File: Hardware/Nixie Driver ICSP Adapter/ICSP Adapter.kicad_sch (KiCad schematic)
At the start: 5 parts

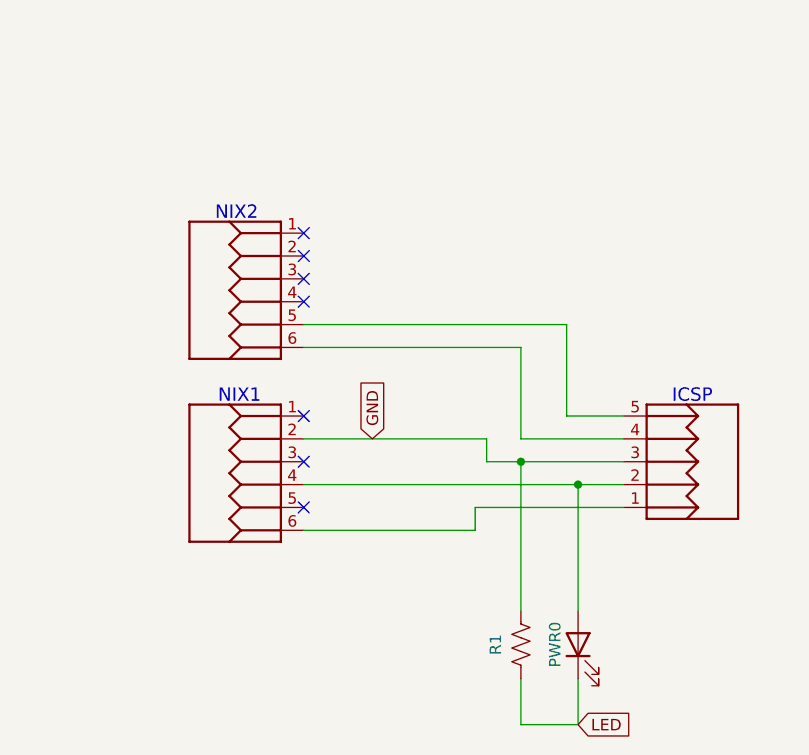
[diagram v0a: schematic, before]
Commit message: Converted to native KiCad footprints and symbols
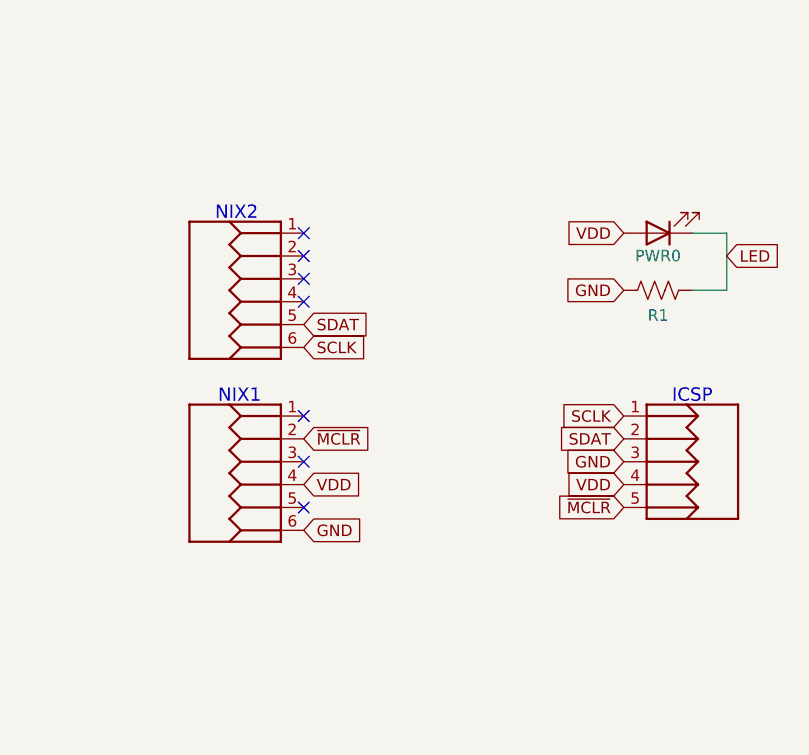
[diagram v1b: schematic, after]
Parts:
- ICSP0: footprint ICSP Adapter:HDR-1X5H -> Connector_PinHeader_2.54mm:PinHeader_1x05_P2.54mm_Horizontal
- NIX1, NIX2: footprint ICSP Adapter:HDRF-2X3 -> Connector_PinHeader_2.54mm:PinHeader_2x03_P2.54mm_Vertical
- PWR0: footprint ICSP Adapter:LED-5MM_ROUND_GREEN -> LED_THT:LED_D5.0mm
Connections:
- net GND: now also NIX1.6 (P6); no longer NIX1.2 (P2)
- net VDD: now reaches NIX1.4 (P4), PWR0.2 (A)
- net VDD: now also ICSP0.4 (P4); no longer ICSP0.2 (P2)
- net SCLK: now reaches ICSP0.1 (P1)
- net SCLK: now also NIX2.6 (P6); no longer NIX1.6 (P6)
- net SDAT: now reaches NIX2.5 (P5)
- net SDAT: now also ICSP0.2 (P2); no longer ICSP0.5 (P5)
- new net ~{MCLR}: ICSP0.5 (P5), NIX1.2 (P2)
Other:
- moved on the sheet: PWR0, R1

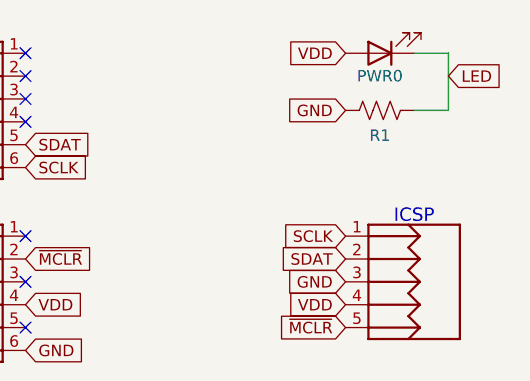
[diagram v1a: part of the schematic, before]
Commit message: Modified ICSP header footprint
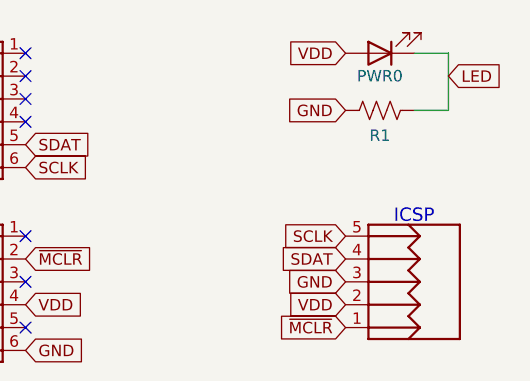
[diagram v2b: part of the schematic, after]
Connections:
- net SCLK: now also ICSP0.5 (P5); no longer ICSP0.1 (P1)
- net SDAT: now also ICSP0.4 (P4); no longer ICSP0.2 (P2)
- net VDD: now also ICSP0.2 (P2); no longer ICSP0.4 (P4)
- net ~{MCLR}: now also ICSP0.1 (P1); no longer ICSP0.5 (P5)
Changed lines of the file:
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@@
 	(symbol
 		(lib_id "ICSP Adapter-eagle-import:HDR-1X5H")
-		(at 171.45 99.06 0)
-		(mirror y)
+		(at 171.45 99.06 180)
 		(unit 1)
 		(exclude_from_sim no)

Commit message: V2 ICSP adapter
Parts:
- removed NIX1, NIX2: HDRF-2X3, Connector_PinHeader_2.54mm:PinHeader_2x03_P2.54mm_Vertical, symbol ICSP Adapter-eagle-import:HDRF-2X3
- added L2: DAT, LED_THT:LED_D5.0mm, symbol Device:LED
- added N1: ~, Nixie:Nixie Driver V2, symbol Nixie:Nixie_Driver
- added R2: 100, Resistor_THT:R_Axial_DIN0207_L6.3mm_D2.5mm_P7.62mm_Horizontal, symbol Device:R_US
- J1: renamed from ICSP0; value HDR-1X5H -> ICSP; symbol ICSP Adapter-eagle-import:HDR-1X5H -> Connector_Generic:Conn_01x05
- L1: renamed from PWR0; value LED-5MM_ROUND_GREEN -> PWR
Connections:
- net GND: now also N1.10 (GND), R2.2
- net SCLK: now also J1.1 (Pin_1), N1.6 (ADDR1); no longer J1.5 (P5)
- net SDAT: now also J1.2 (Pin_2), L2.2 (A), N1.7 (ADDR0); no longer J1.4 (P4)
- net VDD: now also J1.4 (Pin_4), N1.9 (Vdd); no longer J1.2 (P2)
- net ~{MCLR}: now also J1.5 (Pin_5), N1.1 (~{MCLR}); no longer J1.1 (P1)
- net LED: no longer names the net of L1.1 (K), R1.1
- new net: L2.1 (K), R2.1
- no-connect marks 7 -> 5
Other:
- note removed: "ICSP"
- note removed: "NIX1"
- note removed: "NIX2"

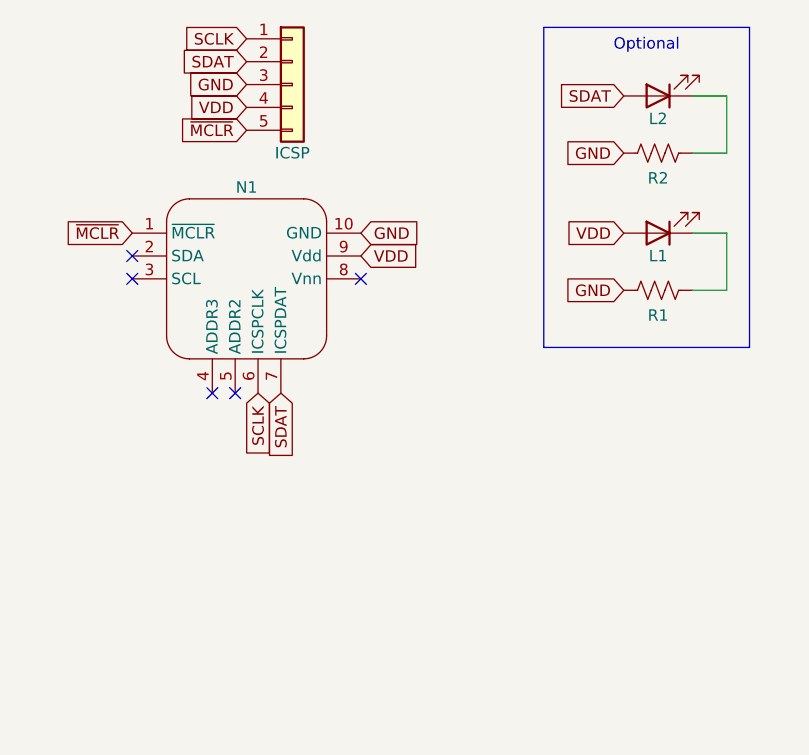
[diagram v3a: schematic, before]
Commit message: Use symbol/footprint fields.
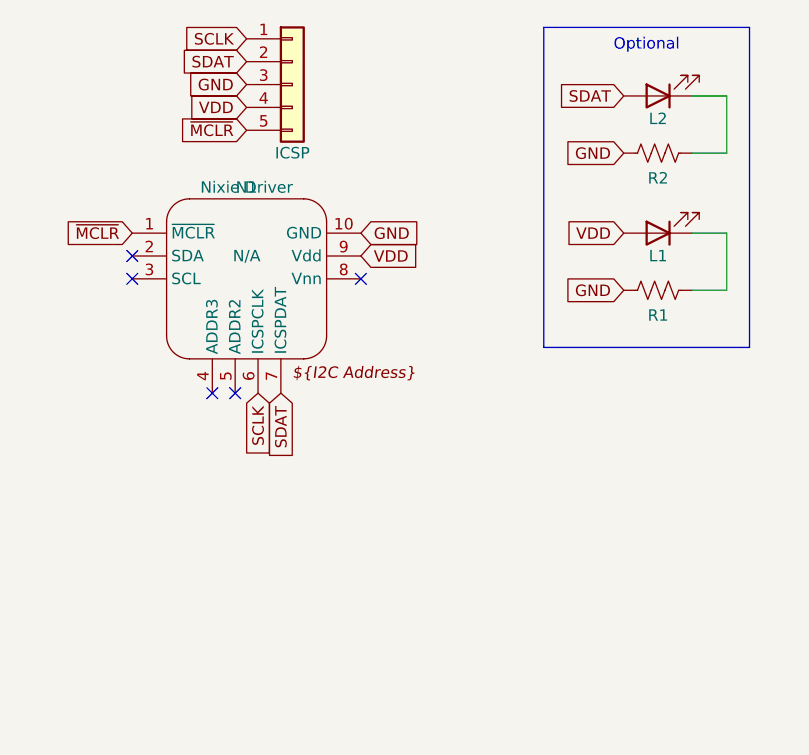
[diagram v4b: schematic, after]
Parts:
- N1: value ~ -> Nixie Driver; I2C Address (none) -> N/A
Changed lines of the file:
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@@
 			)
 		)
-		(property "Value" "~"
+		(property "Value" "Nixie Driver"
 			(at 121.92 68.58 0)
 			(effects
@@
 			)
 		)
+		(property "I2C Address" "N/A"
+			(at 121.92 76.2 0)
+			(effects
+				(font
+					(size 1.27 1.27)
+				)
+			)
+		)
